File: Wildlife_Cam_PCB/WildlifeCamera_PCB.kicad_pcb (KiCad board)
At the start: 2 copper layers, 20 parts, among them J1 PIR, J2 TRIG, Q1 2N3904, SW1 SPST, U1 BQ24210, U3 MCP1703

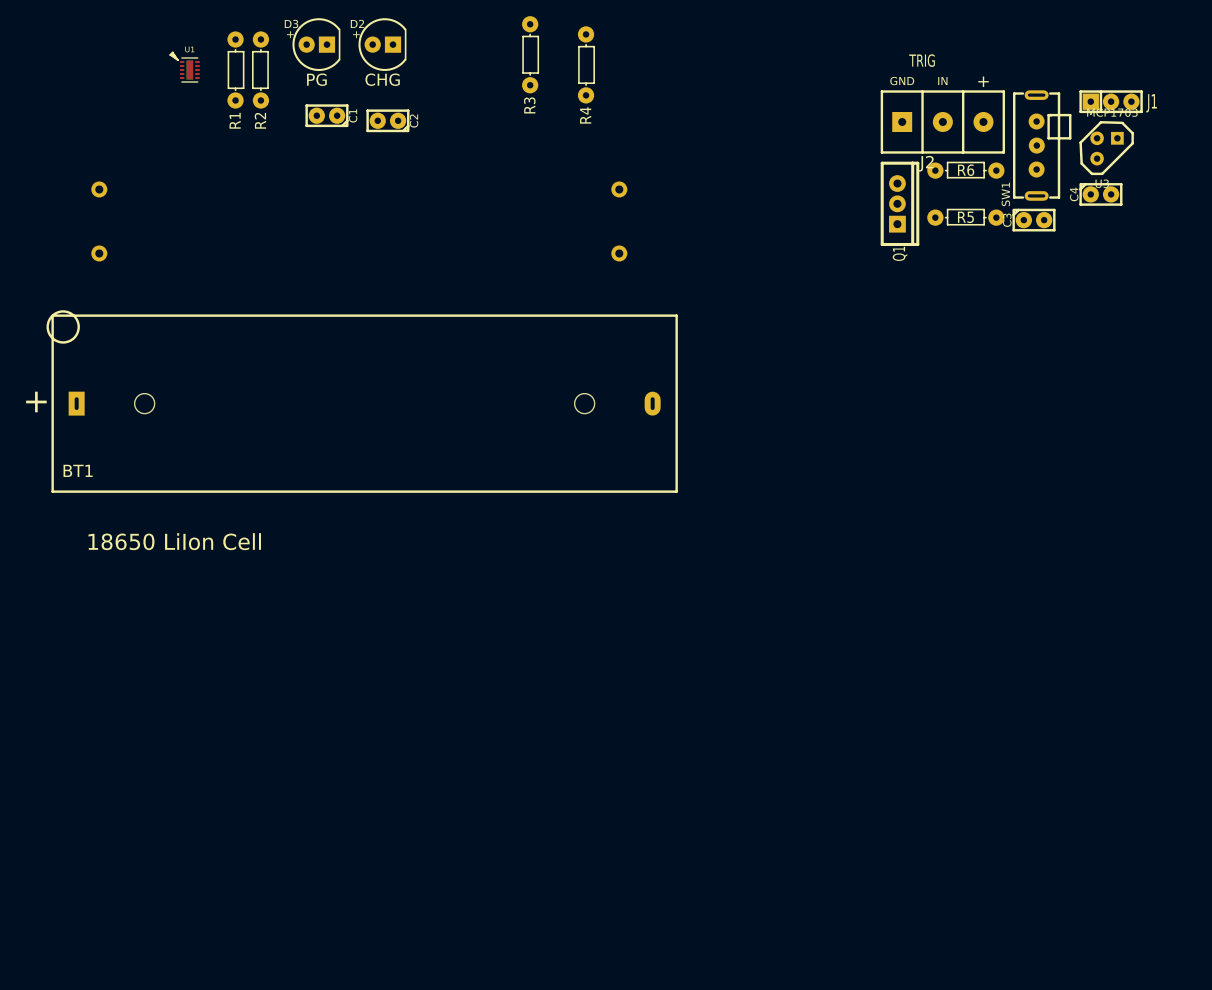
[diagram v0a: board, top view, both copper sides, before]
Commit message: PCB update
Sorted most footprints. Put Items in correct places. Not yet routed
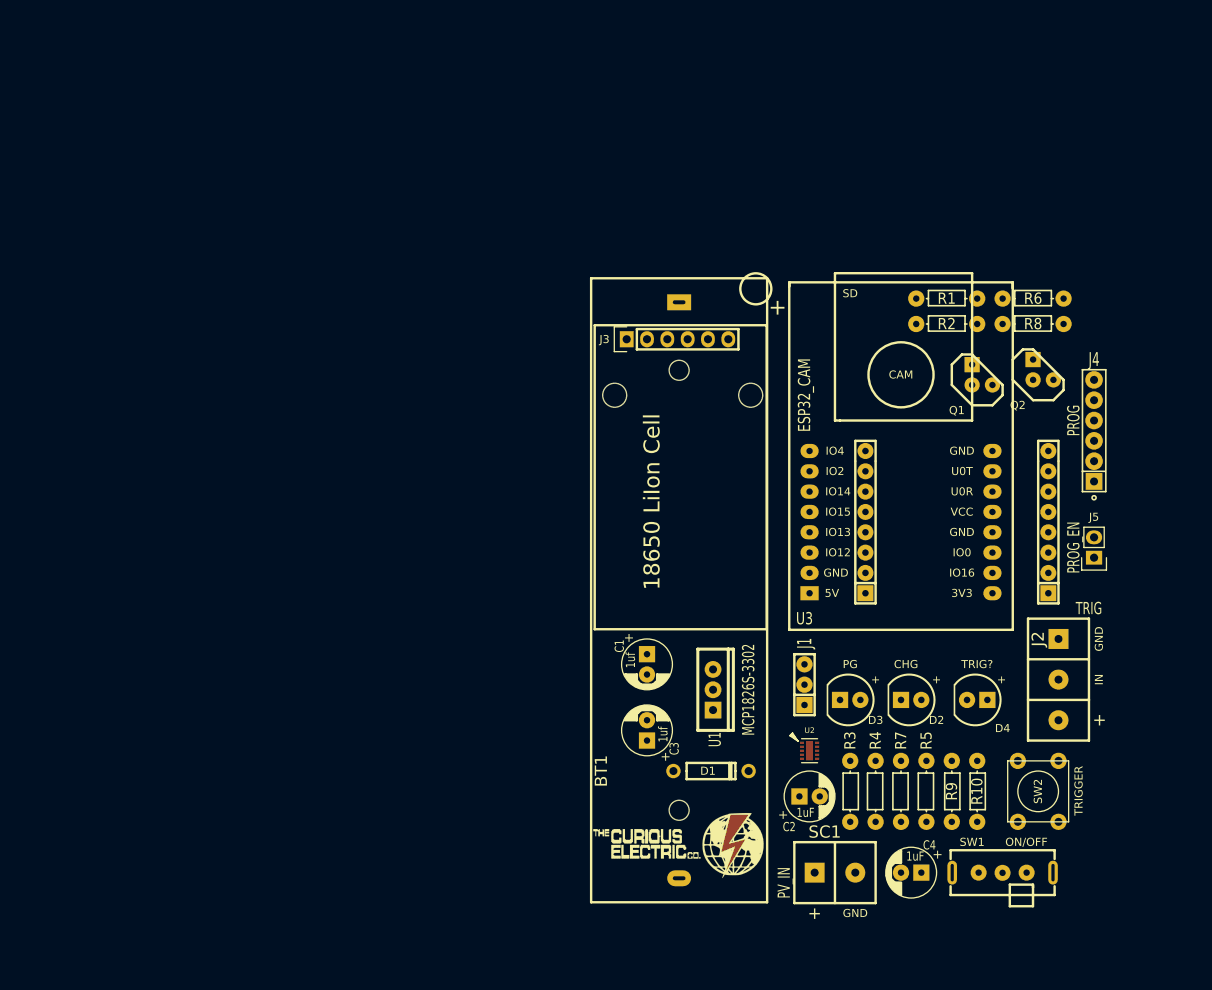
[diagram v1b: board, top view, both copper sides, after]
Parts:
- added D1: ZENER, REInnovationFootprint:TH_Diode_3, F.Cu at (125.7, 116.2)
- added D4: TRIG?, REInnovationFootprint:TH_LED-5MM, F.Cu at (159.4, 107.3)
- added J10: PINS2, REInnovationFootprint:TH_SIL-8_large_pads, F.Cu at (145.4, 86.4)
- added J11: PINS2, REInnovationFootprint:TH_SIL-8_large_pads, F.Cu at (168.3, 86.4)
- added J3: RTC_DS3231, REInnovationFootprint:TH_RTC_MODULE, F.Cu at (115.6, 62.2)
- added J4: PROG, REInnovationFootprint:TH_6x1_CONN, F.Cu at (174.0, 73.7)
- added J5: PROG_EN, REInnovationFootprint:TH_Pin_Header_Straight_1x02, F.Cu at (174.0, 89.5)
- added J6: LOGO1, CuriousElectric3:TCEC_Words_13mm, F.Cu at (111.1, 123.2)
- added J7: LOGO2, CuriousElectric3:2019_011_16_CuriousElectricCompany_Logo_Round_Logo_No_words_KiCAD_10mm_PCBLogo, B.Cu at (129.5, 129.5)
- added Q2: 2N3904, REInnovationFootprint:TO92-EBC_large_pad, F.Cu at (167.6, 66.0)
- added R2: 10k, REInnovationFootprint:TH_Resistor_1, F.Cu at (155.6, 60.3)
- added R6: 1k, REInnovationFootprint:TH_Resistor_1, F.Cu at (166.4, 57.1)
- added R8: 10k, REInnovationFootprint:TH_Resistor_1, F.Cu at (166.4, 60.3)
- added R9: 330, REInnovationFootprint:TH_Resistor_1, F.Cu at (156.2, 118.7)
- added SW2: TRIGGER, REInnovationFootprint:SW_PUSH_SMALL_lg_pad, F.Cu at (167.0, 118.7)
- added U2: BQ24210, REInnovationFootprint:SM_WSON-10-2x3, F.Cu at (138.4, 113.7)
- C1: value 1uF -> 1uf; footprint REInnovationFootprint:C1_lg_pad -> REInnovationFootprint:C_1V7_TH
- C2: footprint REInnovationFootprint:C1_lg_pad -> REInnovationFootprint:C_1V7_TH
- C3: value 1u -> 1uf; footprint REInnovationFootprint:C1_lg_pad -> REInnovationFootprint:C_1V7_TH
- C4: value 1u -> 1uF; footprint REInnovationFootprint:C1_lg_pad -> REInnovationFootprint:C_1V7_TH
- Q1: footprint REInnovationFootprint:TO220_BD135 -> REInnovationFootprint:TO92-EBC_large_pad
- SC1: value PV <2W 5.5V -> PV_IN; footprint REInnovationFootprint:PV_130mmx65mm_NoOutline -> REInnovationFootprint:SIL-2_screw_terminal
- SW1: value SPST -> ON/OFF
- U1: value BQ24210 -> MCP1826S-3302; footprint REInnovationFootprint:SM_WSON-10-2x3 -> REInnovationFootprint:TO220_MCP1826S
- U3: value MCP1703 -> ESP32_CAM; footprint REInnovationFootprint:TH_TO92_MCP1703 -> REInnovationFootprint:ESP32_CAM
- moved SC1 131.4 mm to (139.1, 128.9)
- moved R4 118.5 mm to (146.7, 118.7)
- moved R3 118.5 mm to (143.5, 118.7)
- moved D3 105.6 mm to (143.5, 107.3), turned to 180 degrees
- moved D2 105.2 mm to (151.1, 107.3), turned to 180 degrees
- moved R5 104.6 mm to (153.0, 118.7), turned to 90 degrees
- moved U1 101.4 mm to (126.4, 106.0)
- moved C2 99.6 mm to (138.4, 119.4), turned to 0 degrees
- moved R7 99.0 mm to (149.9, 118.7), turned to 90 degrees
- moved SW1 91.0 mm to (162.6, 128.9), turned to 270 degrees
- moved C4 88.0 mm to (151.1, 128.9), turned to 180 degrees
- moved J1 82.3 mm to (137.8, 105.4), turned to 90 degrees
- moved C3 80.1 mm to (118.1, 111.1), turned to 90 degrees
- moved C1 79.4 mm to (118.1, 102.9), turned to 270 degrees
- moved R10 77.6 mm to (159.4, 118.7), turned to 270 degrees
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- renumbered R5 to R1, R6 to R10, R1 to R3, R2 to R4, R3 to R5, R4 to R7
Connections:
- net Net-(Q1-Pad2) renamed /TRIG
- C2 pad 1: VCC -> Net-(C2-Pad1)
- C3 pad 1: Net-(C3-Pad1) -> +3V3
- C4 pad 1: +3V3 -> VCC
- J2 pad 1: Net-(J2-Pad1) -> GND
- J2 pad 3: Net-(J2-Pad3) -> +3V3
- R10 pad 1: Net-(R6-Pad1) -> Net-(J10-Pad4)
- R3 pad 1: Net-(R1-Pad1) -> Net-(R3-Pad1)
- R4 pad 1: Net-(R2-Pad1) -> Net-(R4-Pad1)
- R4 pad 2: Net-(R2-Pad2) -> Net-(R4-Pad2)
- SC1 pad 1: Net-(C1-Pad1) -> Net-(C2-Pad1)
- SW1 pad 2: Net-(C3-Pad1) -> Net-(C1-Pad1)
- U1 pad 2: Net-(R1-Pad1) -> GND
- U1 pad 3: GND -> +3V3

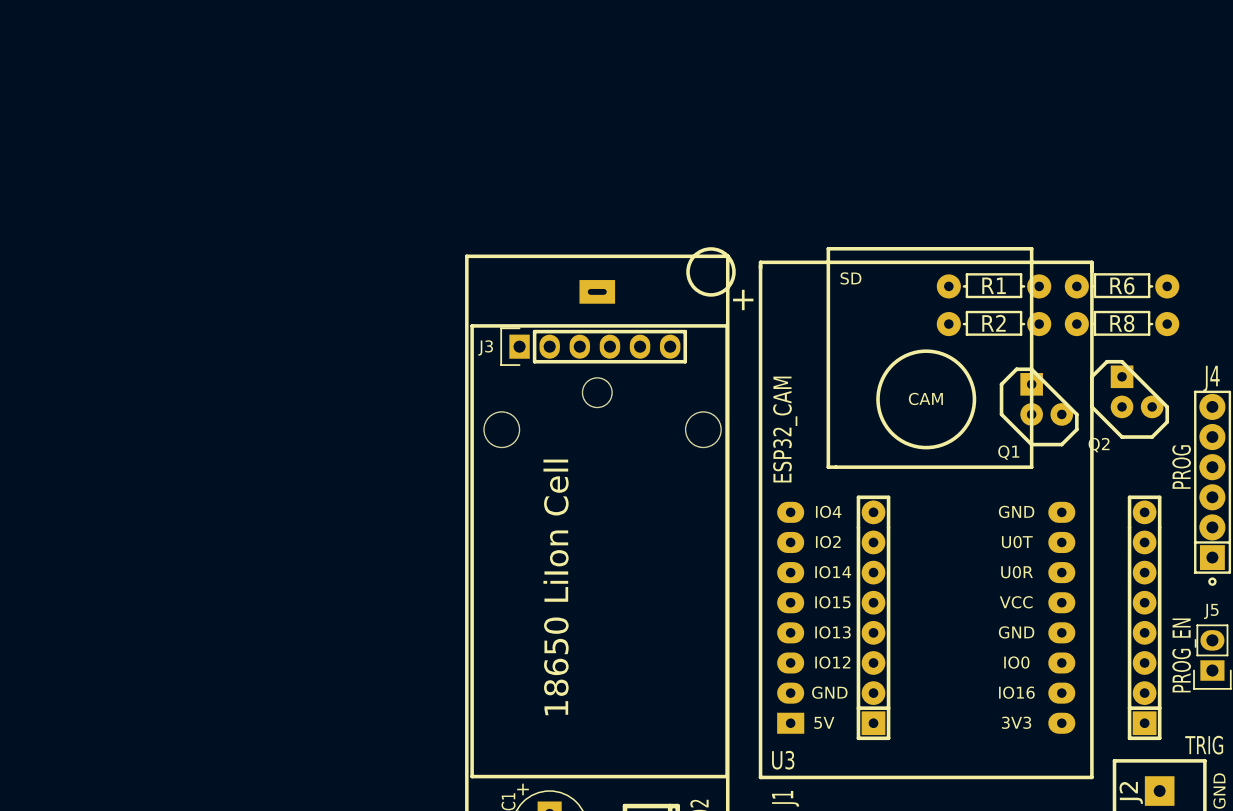
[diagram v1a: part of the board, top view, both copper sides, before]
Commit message: Updated firmware with SD error logging
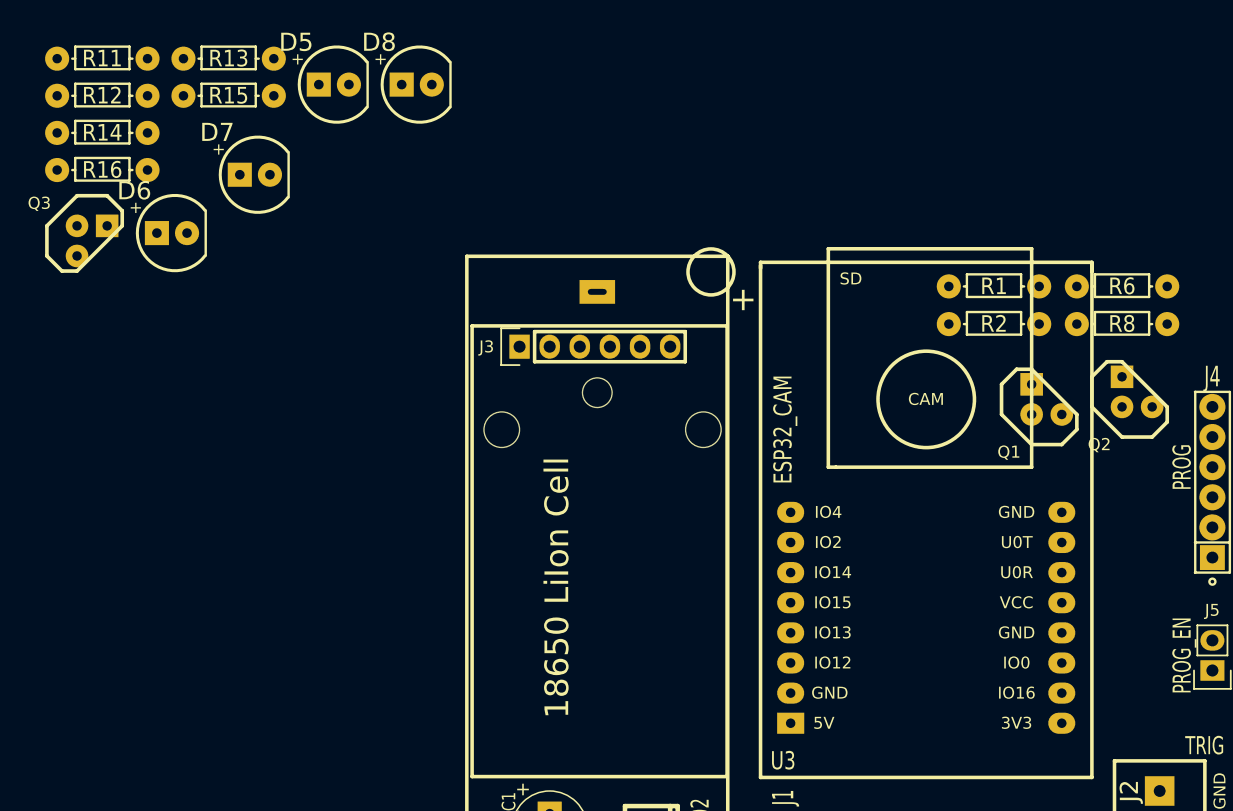
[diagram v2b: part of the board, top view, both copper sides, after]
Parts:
- removed J10, J11: PINS2, REInnovationFootprint:TH_SIL-8_large_pads
- added D5: FLASH, REInnovationFootprint:TH_LED-5MM, F.Cu at (99.9, 40.1)
- added D6: FLASH, REInnovationFootprint:TH_LED-5MM, F.Cu at (86.3, 52.7)
- added D7: FLASH, REInnovationFootprint:TH_LED-5MM, F.Cu at (93.3, 47.7)
- added D8: FLASH, REInnovationFootprint:TH_LED-5MM, F.Cu at (106.9, 40.1)
- added Q3: 2N3904, REInnovationFootprint:TO92-EBC_large_pad, F.Cu at (79.5, 53.3)
- added R11: 1k, REInnovationFootprint:TH_Resistor_1, F.Cu at (80.4, 37.9)
- added R12: 10k, REInnovationFootprint:TH_Resistor_1, F.Cu at (80.4, 41.1)
- added R13: 100, REInnovationFootprint:TH_Resistor_1, F.Cu at (91.0, 37.9)
- added R14: 100, REInnovationFootprint:TH_Resistor_1, F.Cu at (80.4, 44.2)
- added R15: 100, REInnovationFootprint:TH_Resistor_1, F.Cu at (91.0, 41.1)
- added R16: 100, REInnovationFootprint:TH_Resistor_1, F.Cu at (80.4, 47.3)

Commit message: Update of PCB
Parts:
- added J8: PCB, REInnovationFootprint:PCB_Wildlife_Cam, F.Cu at (198.8, 146.1)
- D5, D6, D7, D8, J1: moved to B.Cu
- J3: footprint REInnovationFootprint:TH_RTC_MODULE -> REInnovationFootprint:TH_RTC_MODULE_SM
- Q3: value 2N3904 -> BD135; footprint REInnovationFootprint:TO92-EBC_large_pad -> REInnovationFootprint:TO220_BD135
- SC1: footprint REInnovationFootprint:SIL-2_screw_terminal -> REInnovationFootprint:SIL_2_screw_+_JST_2mm
- moved R16 100.6 mm to (171.4, 90.2)
- moved R14 99.3 mm to (171.4, 83.8)
- moved R15 92.6 mm to (171.4, 87.0)
- moved R13 91.0 mm to (171.4, 80.6)
- moved R12 89.5 mm to (153.0, 93.3), turned to 90 degrees
- moved R11 88.9 mm to (149.9, 93.3), turned to 270 degrees
- moved Q3 86.2 mm to (156.8, 91.4)
- moved D8 84.9 mm to (161.9, 104.8)
- moved D7 83.1 mm to (153.7, 104.8)
- moved D6 78.8 mm to (145.4, 104.8)
- moved D5 74.9 mm to (137.8, 104.8)
- moved J6 62.9 mm to (109.9, 60.3), turned to 270 degrees
- moved J3 61.3 mm to (176.5, 55.9), turned to 180 degrees
- moved J7 58.9 mm to (148.6, 73.8)
- moved C3 51.2 mm to (168.3, 121.3), turned to 0 degrees
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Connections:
- D1 pad 2: +3V3 -> GND
- J3 pad 1: Net-(J3-Pad1) -> +3V3
- J3 pad 2: /ALARM -> /I2C_DAT
- J3 pad 4: /I2C_DAT -> Net-(J3-Pad4)
- J3 pad 5: +3V3 -> GND
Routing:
- net GND: track 0.00 -> 299.4 mm
- net +3V3: track 0.00 -> 182.7 mm
- net VCC: track 0.00 -> 155.9 mm
- net Net-(D1-Pad1): track 0.00 -> 92.4 mm, vias 0 -> 1
- net /PROG_EN: track 0.00 -> 86.8 mm
- net /TRIG: track 0.00 -> 75.5 mm
- net Net-(D3-Pad1): track 0.00 -> 62.9 mm
- net Net-(J1-Pad2): track 0.00 -> 60.5 mm, vias 0 -> 2
- net /U0T: track 0.00 -> 49.3 mm, vias 0 -> 1
- net /U0R: track 0.00 -> 48.9 mm, vias 0 -> 1
- net Net-(D3-Pad2): track 0.00 -> 48.9 mm
- net Net-(D5-Pad2): track 0.00 -> 48.7 mm
- net Net-(R10-Pad1): track 0.00 -> 48.0 mm
- net Net-(D2-Pad2): track 0.00 -> 46.9 mm
- net /I2C_CLK: track 0.00 -> 46.7 mm, vias 0 -> 1
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- added copper zone on B.Cu, net GND
- added copper zone on F.Cu, net GND
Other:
- board outline added: 79.8 x 84.8 mm
- board text added: "31/10/2020 v1"
- board text added: "@curiouselectric"
- board text added: "FLASH"
- board text added: "PIR"
- board text added: "WildLife ESP CAM"
- board text added: "www.curiouselectric.co.uk"

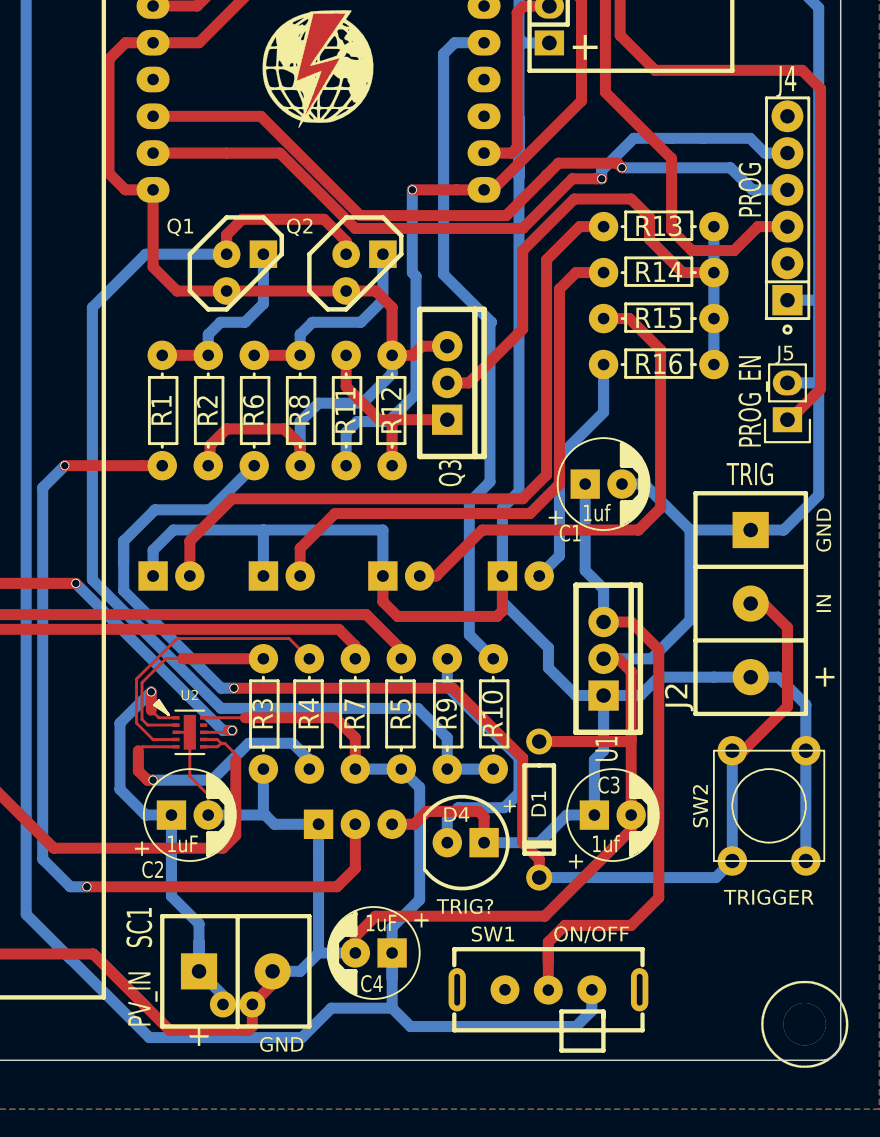
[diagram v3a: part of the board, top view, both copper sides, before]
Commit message: Update of code - sorting libraries
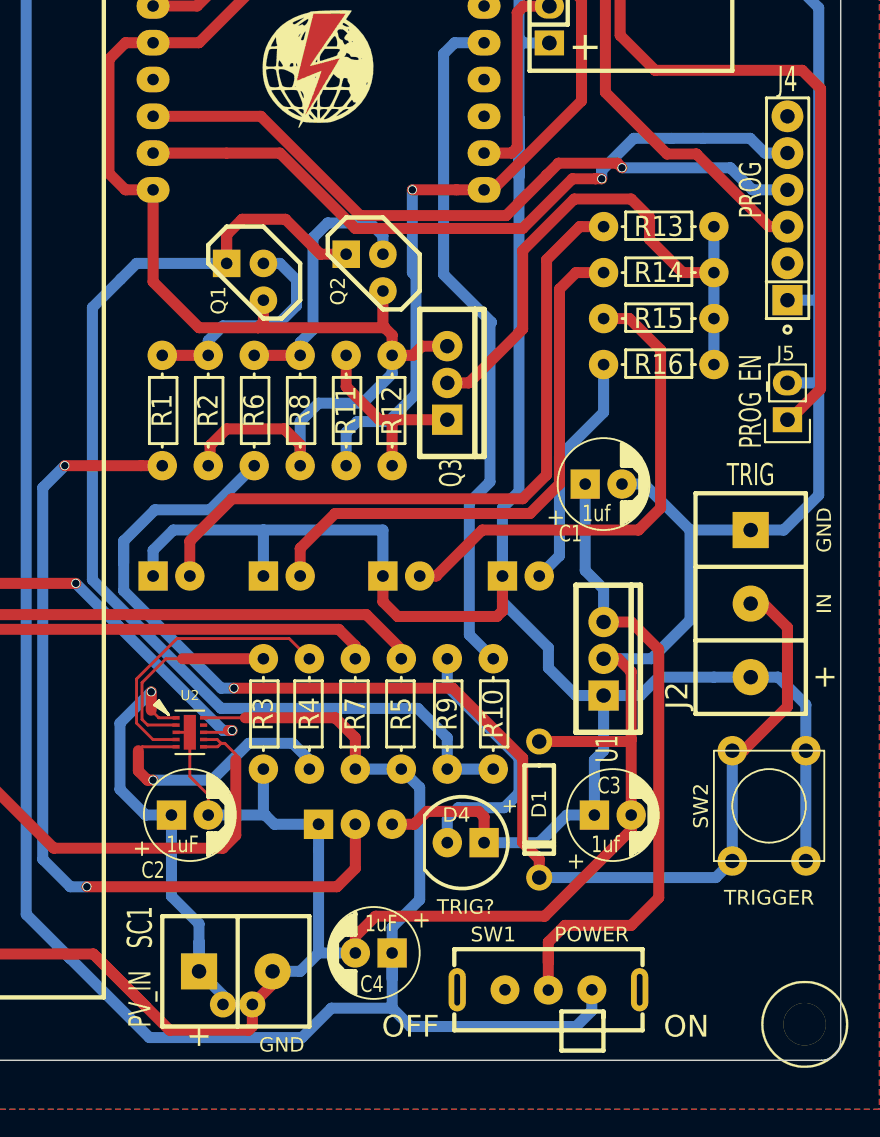
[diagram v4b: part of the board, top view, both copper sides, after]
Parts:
- J1: footprint REInnovationFootprint:SIL-3_lg_pad -> REInnovationFootprint:SIL-3_PIR_SENSOR
- Q1, Q2: footprint REInnovationFootprint:TO92-EBC_large_pad -> REInnovationFootprint:NPN_BC337
- SW1: value ON/OFF -> POWER
- moved Q1 0.64 mm to (142.9, 84.5), turned to 270 degrees
- turned Q2 to 270 degrees
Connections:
- Q1 pad 1: Net-(Q1-Pad1) -> /TRIG
- Q1 pad 2: /TRIG -> Net-(Q1-Pad2)
- Q2 pad 1: Net-(Q2-Pad1) -> /TRIG
- Q2 pad 2: /TRIG -> Net-(Q2-Pad2)
- R1 pad 1: Net-(Q1-Pad1) -> Net-(Q1-Pad2)
- R2 pad 1: Net-(Q1-Pad1) -> Net-(Q1-Pad2)
- R6 pad 1: Net-(Q2-Pad1) -> Net-(Q2-Pad2)
- R8 pad 1: Net-(Q2-Pad1) -> Net-(Q2-Pad2)
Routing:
- net Net-(Q2-Pad2): track 0.00 -> 18.6 mm
- net Net-(Q1-Pad2): track 0.00 -> 15.8 mm
- net Net-(Q2-Pad1): track 14.5 -> 0.00 mm
- net Net-(Q1-Pad1): track 12.7 -> 0.00 mm
- net /5V_PWR: track 46.6 -> 42.3 mm
- net GND: track 299.4 -> 303.6 mm
- net /TRIG: track 75.5 -> 76.7 mm
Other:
- board text added: "OFF"
- board text added: "ON"
- board text removed: "PIR"
